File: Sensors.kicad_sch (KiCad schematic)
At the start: 27 parts, among them U11 DRV5023AJxDBZ, U18 LTR-303ALS-01, U21 HP203B, U22 SPH0645LM4H, U29 SGP30, U7 BME280

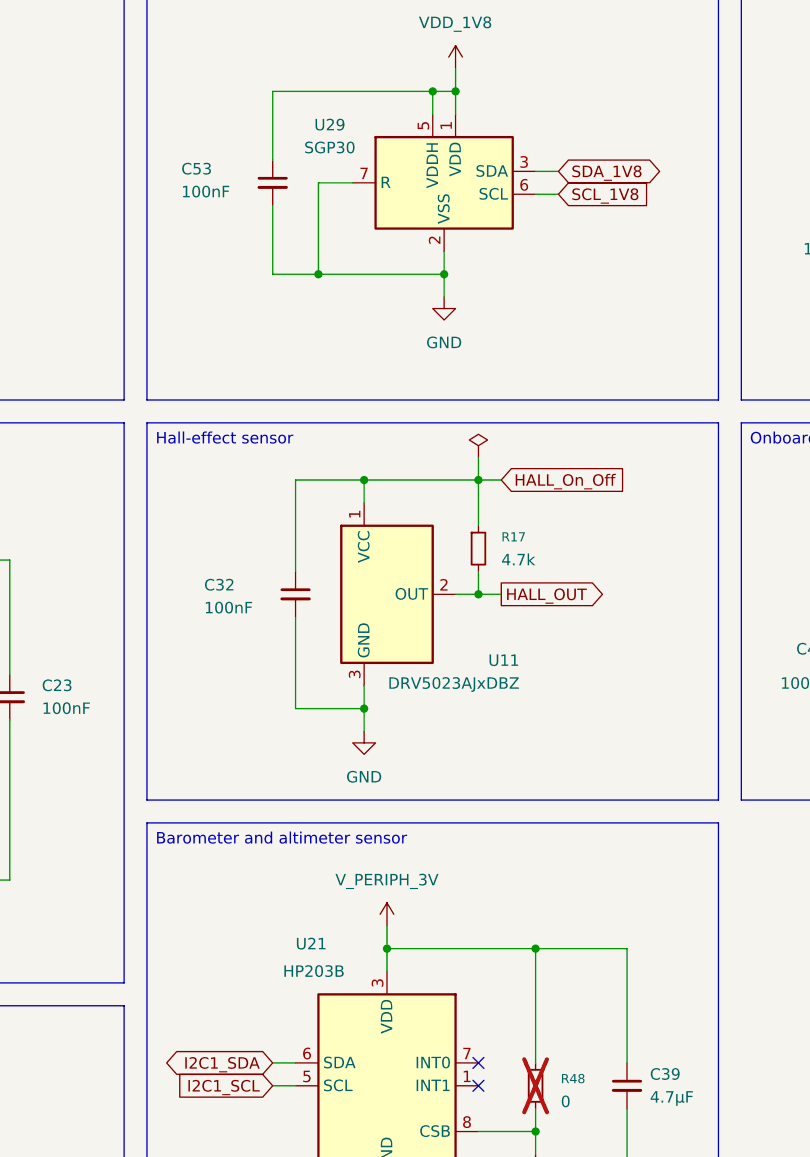
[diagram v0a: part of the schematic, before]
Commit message: PCB component placement according to AIoT2
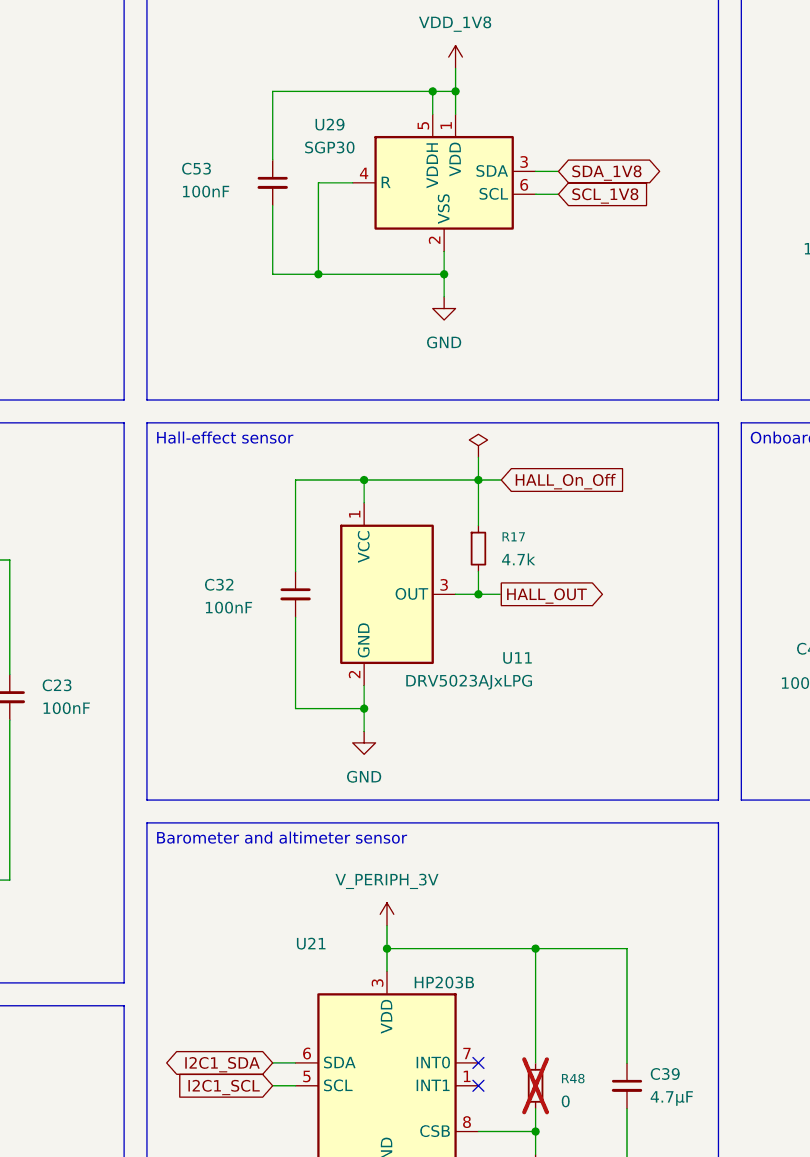
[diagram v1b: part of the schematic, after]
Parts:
- removed U11: DRV5023AJxDBZ, Package_TO_SOT_SMD:SOT-23, symbol Sensor_Magnetic:DRV5033AJxDBZ
- added U11: DRV5023AJxLPG, Package_TO_SOT_THT:TO-92_Inline, symbol Sensor_Magnetic:DRV5033AJxLPG
- U21: footprint Package_LGA:NXP_LGA-8_3x5mm_P1.25mm_H1.1mm -> footprints:LGA-8_3.6x3.8mm_P0.9mm
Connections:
- net GND: now also U29.4 (R), U11.2 (GND); no longer U29.9 (VSS)
- net HALL_OUT: now also U11.3 (OUT)
- net HALL_On_Off: now also U11.1 (VCC)
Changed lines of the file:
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@@
 		(pin "7"
 		)
-		(pin "9"
+		(pin "4"
 		)
 		(instances
@@
 	)
 	(symbol
+		(lib_id "Sensor_Magnetic:DRV5033AJxLPG")
+		(at 137.16 86.36 0)
+		(unit 1)
+		(body_style 1)
+		(exclude_from_sim no)
+		(in_bom yes)
+		(on_board yes)
+		(in_pos_files yes)
+		(dnp no)
+		(property "Reference" "U11"
+			(at 153.416 93.472 0)
+			(show_name no)
+			(do_not_autoplace no)
+			(effects
+				(font
+					(size 1.27 1.27)
+				)
+				(justify right)
+			)
+		)
+		(property "Value" "DRV5023AJxLPG"
+			(at 153.416 96.012 0)
+			(show_name no)
+			(do_not_autoplace no)
+			(effects
+				(font
+					(size 1.27 1.27)
+				)
+				(justify right)
+			)
+		)
+		(property "Footprint" "Package_TO_SOT_THT:TO-92_Inline"
+			(at 137.16 86.36 0)
+			(hide yes)
+			(show_name no)
+			(do_not_autoplace no)
+			(effects
+				(font
+					(size 1.27 1.27)
+				)
+			)
+		)
+		(property "Datasheet" "https://www.ti.com/lit/ds/symlink/drv5033.pdf"
+			(at 137.16 86.36 0)
+			(hide yes)
+			(show_name no)
+			(do_not_autoplace no)
+			(effects
+				(font
+					(size 1.27 1.27)
+				)
+			)
+		)
+		(property "Description" "±6.9 / ±3.5 mT, 20-kHz, 2-38V, TO-92"
+			(at 137.16 86.36 0)
+			(hide yes)
+			(show_name no)
+			(do_not_autoplace no)
+			(effects
+				(font
+					(size 1.27 1.27)
+				)
+			)
+		)
+		(pin "2"
+		)
+		(pin "3"
+		)
+		(pin "1"
+		)
+		(instances
+			(project "uca-dkaiot2-kicad"
+				(path "/13b7de53-ecff-4b32-b513-b5b471d022a3/14d734f9-3275-482e-9982-51867d0b2093"
+					(reference "U11")
+					(unit 1)
+				)
+			)
+		)
+	)
+	(symbol
 		(lib_id "Sensor_Optical:LTR-303ALS-01")
 		(at 59.69 41.91 0)
@@
 		)
 		(property "Value" "HP203B"
-			(at 129.032 128.27 0)
-			(show_name no)
-			(do_not_autoplace no)
-			(effects
-				(font
-					(size 1.27 1.27)
-				)
-			)
-		)
-		(property "Footprint" "Package_LGA:NXP_LGA-8_3x5mm_P1.25mm_H1.1mm"
+			(at 143.51 129.54 0)
+			(show_name no)
+			(do_not_autoplace no)
+			(effects
+				(font
+					(size 1.27 1.27)
+				)
+			)
+		)
+		(property "Footprint" "footprints:LGA-8_3.6x3.8mm_P0.9mm"
 			(at 162.56 152.4 0)
 			(hide yes)
@@
 				)
 			)
-		)
-	)
-	(symbol
-		(lib_id "Sensor_Magnetic:DRV5033AJxDBZ")
-		(at 137.16 86.36 0)
-		(unit 1)
-		(body_style 1)
-		(exclude_from_sim no)
-		(in_bom yes)
-		(on_board yes)
-		(in_pos_files yes)
-		(dnp no)
-		(property "Reference" "U11"
-			(at 151.892 93.726 0)
-			(show_name no)
-			(do_not_autoplace no)
-			(effects
-				(font
-					(size 1.27 1.27)
-				)
-				(justify right)
-			)
-		)
-		(property "Value" "DRV5023AJxDBZ"
-			(at 151.892 96.266 0)
-			(show_name no)
-			(do_not_autoplace no)
-			(effects
-				(font
-					(size 1.27 1.27)
-				)
-				(justify right)
-			)
-		)
-		(property "Footprint" "Package_TO_SOT_SMD:SOT-23"
-			(at 137.16 86.36 0)
-			(hide yes)
-			(show_name no)
-			(do_not_autoplace no)
-			(effects
-				(font
-					(size 1.27 1.27)
-				)
-			)
-		)
-		(property "Datasheet" "https://www.ti.com/lit/ds/symlink/drv5033.pdf"
-			(at 137.16 86.36 0)
-			(hide yes)
-			(show_name no)
-			(do_not_autoplace no)
-			(effects
-				(font
-					(size 1.27 1.27)
-				)
-			)
-		)
-		(property "Description" "±6.9 / ±3.5 mT, 20-kHz, 2-38V, SOT-23"
-			(at 137.16 86.36 0)
-			(hide yes)
-			(show_name no)
-			(do_not_autoplace no)
-			(effects
-				(font
-					(size 1.27 1.27)
-				)
-			)
-		)
-		(pin "1"
-		)
-		(pin "3"
-		)
-		(pin "2"
-		)
-		(instances
-			(project "uca-dkaiot2-kicad"
-				(path "/13b7de53-ecff-4b32-b513-b5b471d022a3/14d734f9-3275-482e-9982-51867d0b2093"
-					(reference "U11")
-					(unit 1)
-					(variant
-						(name "Ambient")
-						(dnp yes)
-					)
-				)
-			)
